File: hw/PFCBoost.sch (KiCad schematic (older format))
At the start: 15 parts

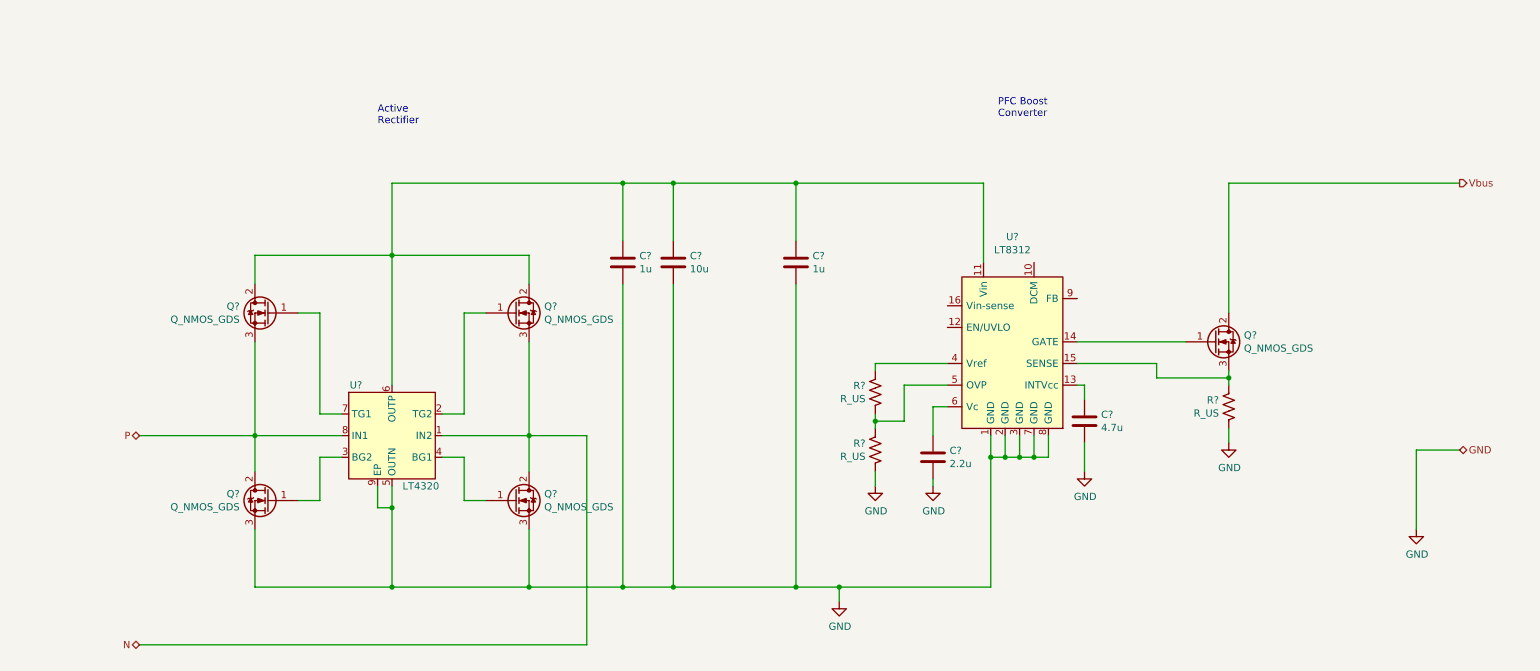
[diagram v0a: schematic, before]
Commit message: More work on PFC
Added more circuitry to PFC boost converter; about half done
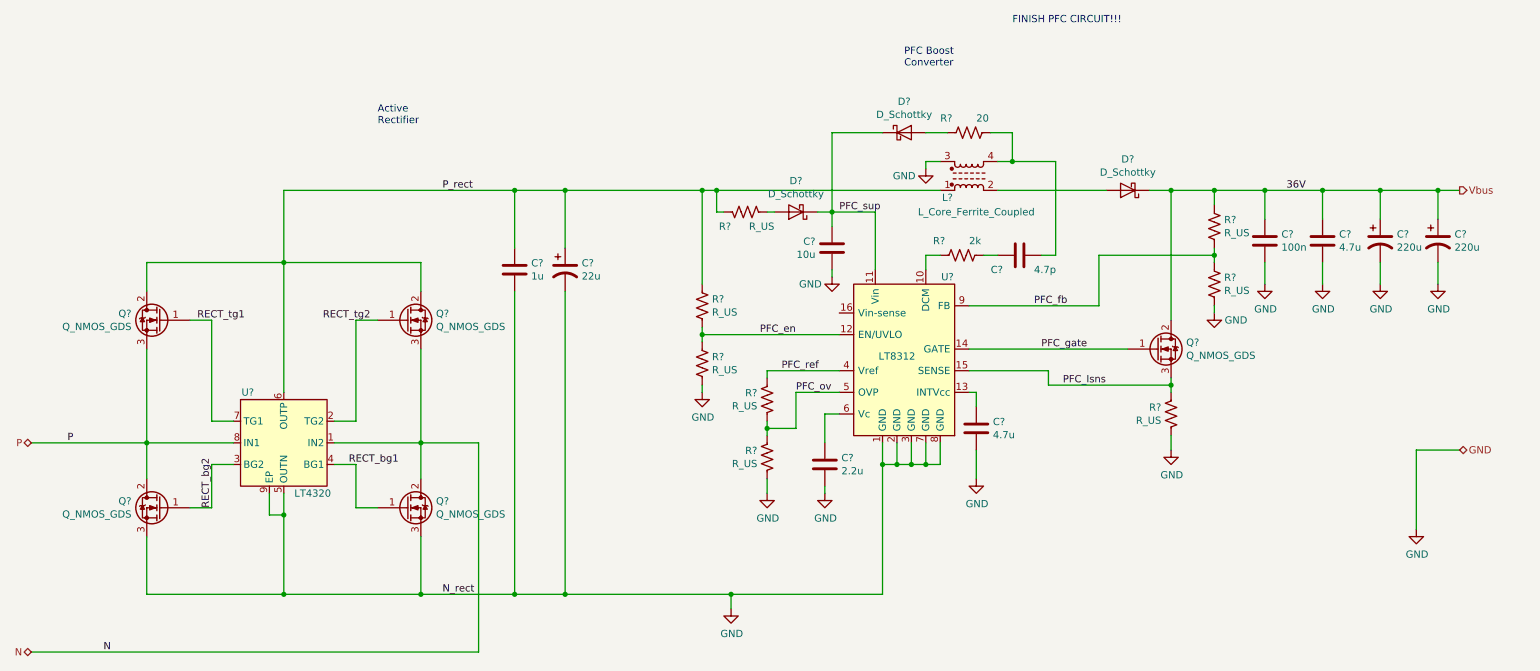
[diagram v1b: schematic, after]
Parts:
- removed C?: 10u, symbol Device:C
- removed C?: 1u, symbol Device:C
- added C?: 100n, Capacitor_SMD:C_0603_1608Metric, symbol Device:C
- added C? (x2): 220u, symbol Device:CP1
- added C?: 22u, symbol Device:CP1
- added C?: 4.7p, symbol Device:C
- added C?: 10u, Capacitor_SMD:C_1210_3225Metric_Pad1.42x2.65mm_HandSolder, symbol Device:C
- added C?: 4.7u, Capacitor_SMD:C_1210_3225Metric_Pad1.42x2.65mm_HandSolder, symbol Device:C
- added D?: D_Schottky, Diode_SMD:D_SMB, symbol Device:D_Schottky
- added D?: D_Schottky, symbol Device:D_Schottky
- added D?: D_Schottky, Diode_SMD:D_SOD-123, symbol Device:D_Schottky
- added L?: L_Core_Ferrite_Coupled, symbol Device:L_Core_Ferrite_Coupled
- added R? (x5): R_US, Resistor_SMD:R_0603_1608Metric, symbol Device:R_US
- added R?: 2k, Resistor_SMD:R_0603_1608Metric, symbol Device:R_US
- added R?: 20, Resistor_SMD:R_0603_1608Metric, symbol Device:R_US
- R?: footprint (none) -> Resistor_SMD:R_0612_1632Metric
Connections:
- net GND: now also C?.2, C?.2, C?.2, C?.2, C?.2, C?.2, L?.3, R?.1, R?.1
- net Vbus: now also C?.1, C?.1, C?.1, C?.1, D?.1 (K), R?.2
- net RECT_tg2: now reaches Q?.1 (G), U?.2 (TG2)
- net RECT_bg2: now reaches Q?.1 (G), U?.3 (BG2)
- net RECT_bg1: now reaches Q?.1 (G), U?.4 (BG1)
- net P_rect: now reaches C?.1, Q?.2 (D), Q?.2 (D), U?.6 (OUTP)
- net P_rect: now also C?.1, L?.1, R?.2, R?.2; no longer U?.11 (Vin)
- net RECT_tg1: now reaches Q?.1 (G), U?.7 (TG1)
- net at U?.10 (DCM): now also R?.1
- net PFC_en: now reaches U?.12 (EN/UVLO)
- net PFC_en: now also R?.1, R?.2
- net PFC_gate: now reaches Q?.1 (G), U?.14 (GATE)
- net PFC_Isns: now reaches Q?.3 (S), R?.2, U?.15 (SENSE)
- net PFC_ref: now reaches R?.2, U?.4 (Vref)
- net PFC_ov: now reaches R?.1, R?.2, U?.5 (OVP)
- net PFC_fb: now reaches U?.9 (FB)
- net PFC_fb: now also R?.1, R?.2
- new net: D?.2 (A), L?.2
- new net: C?.1, L?.4, R?.2
- new net: C?.2, R?.2
- new net: D?.2 (A), R?.1 (x2)
- new net PFC_sup: C?.1, D?.1 (K), D?.1 (K), U?.11 (Vin)
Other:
- note added: "FINISH PFC CIRCUIT!!!"
- moved on the sheet: C?, Q?, R?, U?

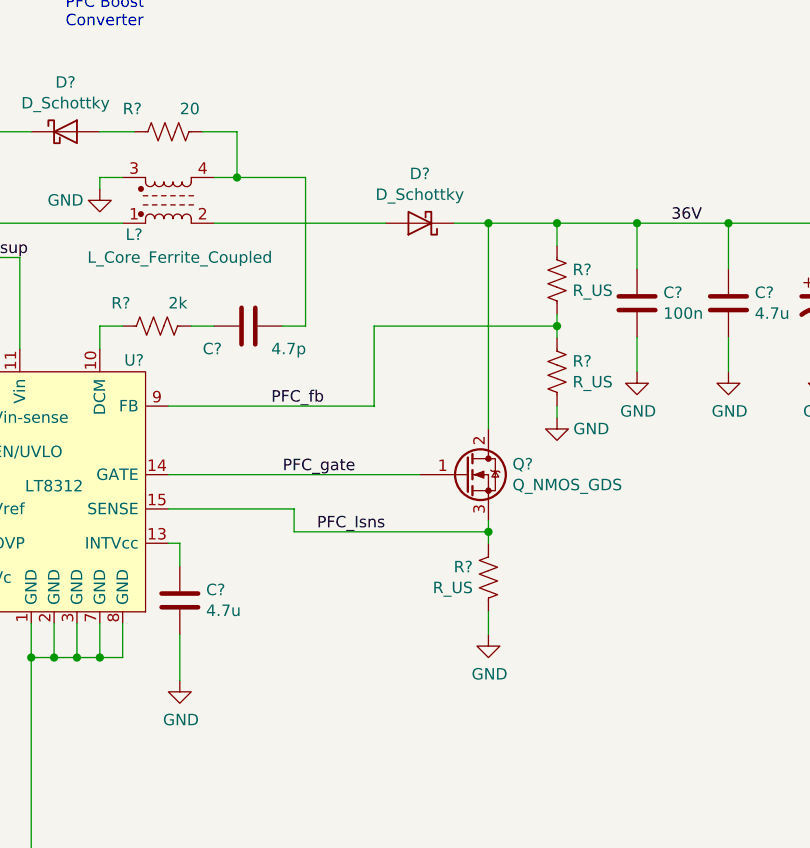
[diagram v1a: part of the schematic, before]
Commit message: Primary SW component selection
selected some components for primary switcher, added AuxOut block, dropped down primary linear reg IC
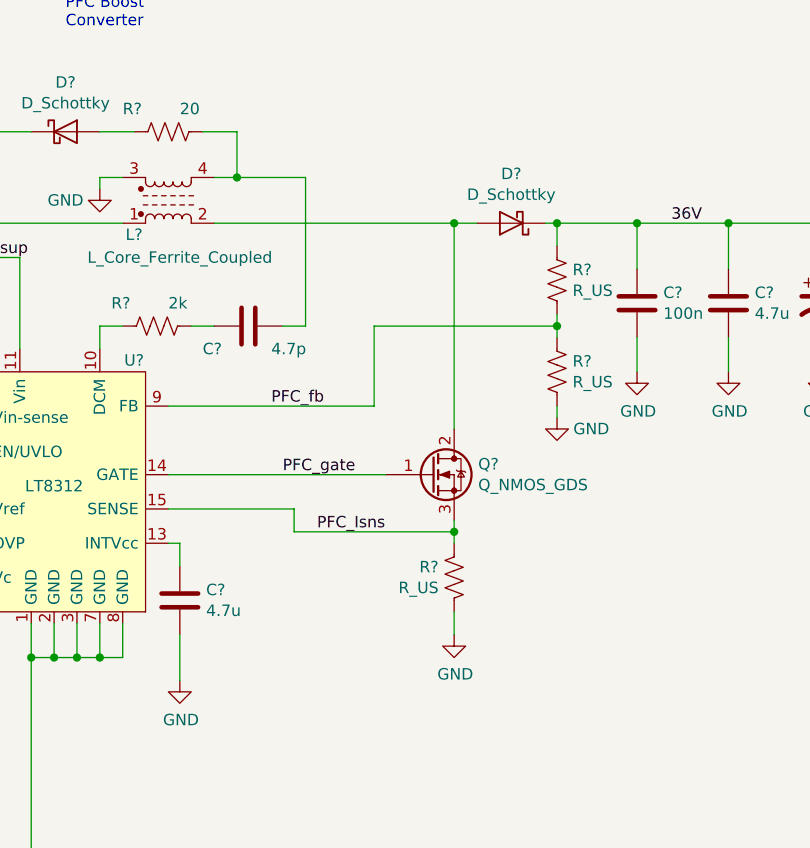
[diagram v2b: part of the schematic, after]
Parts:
- C?: footprint (none) -> Capacitor_SMD:C_0805_2012Metric
- C? (x2): footprint (none) -> Capacitor_SMD:C_0805_2012Metric_Pad1.15x1.40mm_HandSolder
- C?: footprint (none) -> Capacitor_SMD:C_0603_1608Metric
- D?: footprint (none) -> Diode_SMD:D_SOD-123
- R? (x2): footprint (none) -> Resistor_SMD:R_0603_1608Metric
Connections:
- net Vbus: no longer Q?.2 (D)
- net at D?.2 (A), L?.2: now also Q?.2 (D)
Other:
- moved on the sheet: D?, Q?, R?
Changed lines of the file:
@@
 $Descr A4 11693 8268
 encoding utf-8
-Sheet 2 6
+Sheet 2 7
 Title ""
 Date ""
@@
 F 0 "C?" H 4265 2546 50  0000 L CNN
 F 1 "1u" H 4265 2455 50  0000 L CNN
-F 2 "" H 4188 2350 50  0001 C CNN
+F 2 "Capacitor_SMD:C_0805_2012Metric" H 4188 2350 50  0001 C CNN
 F 3 "~" H 4150 2500 50  0001 C CNN
 	1    4150 2500
@@
 F 0 "C?" H 7465 3646 50  0000 L CNN
 F 1 "4.7u" H 7465 3555 50  0000 L CNN
-F 2 "" H 7388 3450 50  0001 C CNN
+F 2 "Capacitor_SMD:C_0805_2012Metric_Pad1.15x1.40mm_HandSolder" H 7388 3450 50  0001 C CNN
 F 3 "~" H 7350 3600 50  0001 C CNN
 	1    7350 3600
@@
 F 0 "R?" H 5832 3754 50  0000 R CNN
 F 1 "R_US" H 5832 3845 50  0000 R CNN
-F 2 "" V 5940 3790 50  0001 C CNN
+F 2 "Resistor_SMD:R_0603_1608Metric" V 5940 3790 50  0001 C CNN
 F 3 "~" H 5900 3800 50  0001 C CNN
 	1    5900 3800
@@
 F 0 "R?" H 5832 3354 50  0000 R CNN
 F 1 "R_US" H 5832 3445 50  0000 R CNN
-F 2 "" V 5940 3390 50  0001 C CNN
+F 2 "Resistor_SMD:R_0603_1608Metric" V 5940 3390 50  0001 C CNN
 F 3 "~" H 5900 3400 50  0001 C CNN
 	1    5900 3400
@@
 F 0 "C?" H 6415 3896 50  0000 L CNN
 F 1 "2.2u" H 6415 3805 50  0000 L CNN
-F 2 "" H 6338 3700 50  0001 C CNN
+F 2 "Capacitor_SMD:C_0805_2012Metric_Pad1.15x1.40mm_HandSolder" H 6338 3700 50  0001 C CNN
 F 3 "~" H 6300 3850 50  0001 C CNN
 	1    6300 3850
@@
 L Device:Q_NMOS_GDS Q?
 U 1 1 5E8395C3
-P 8600 3050
-F 0 "Q?" H 8805 3096 50  0000 L CNN
-F 1 "Q_NMOS_GDS" H 8805 3005 50  0000 L CNN
-F 2 "" H 8800 3150 50  0001 C CNN
-F 3 "~" H 8600 3050 50  0001 C CNN
-	1    8600 3050
+P 8450 3050
+F 0 "Q?" H 8655 3096 50  0000 L CNN
+F 1 "Q_NMOS_GDS" H 8655 3005 50  0000 L CNN
+F 2 "" H 8650 3150 50  0001 C CNN
+F 3 "~" H 8450 3050 50  0001 C CNN
+	1    8450 3050
 	1    0    0    -1
 $EndComp
@@
 L Device:R_US R?
 U 1 1 5E8396C6
-P 8700 3500
-F 0 "R?" H 8632 3454 50  0000 R CNN
-F 1 "R_US" H 8632 3545 50  0000 R CNN
-F 2 "Resistor_SMD:R_0612_1632Metric" V 8740 3490 50  0001 C CNN
-F 3 "~" H 8700 3500 50  0001 C CNN
-	1    8700 3500
+P 8550 3500
+F 0 "R?" H 8482 3454 50  0000 R CNN
+F 1 "R_US" H 8482 3545 50  0000 R CNN
+F 2 "Resistor_SMD:R_0612_1632Metric" V 8590 3490 50  0001 C CNN
+F 3 "~" H 8550 3500 50  0001 C CNN
+	1    8550 3500
 	1    0    0    1
 $EndComp
@@
 L power:GND #PWR?
 U 1 1 5E839706
-P 8700 3750
-F 0 "#PWR?" H 8700 3500 50  0001 C CNN
-F 1 "GND" H 8705 3577 50  0000 C CNN
-F 2 "" H 8700 3750 50  0001 C CNN
-F 3 "" H 8700 3750 50  0001 C CNN
-	1    8700 3750
-	1    0    0    -1
-$EndComp
-Wire Wire Line
-	8700 3250 8700 3300
-Wire Wire Line
-	7300 3050 8400 3050
-Wire Wire Line
-	8700 3300 7850 3300
+P 8550 3750
+F 0 "#PWR?" H 8550 3500 50  0001 C CNN
+F 1 "GND" H 8555 3577 50  0000 C CNN
+F 2 "" H 8550 3750 50  0001 C CNN
+F 3 "" H 8550 3750 50  0001 C CNN
+	1    8550 3750
+	1    0    0    -1
+$EndComp
+Wire Wire Line
+	8550 3250 8550 3300
+Wire Wire Line
+	7300 3050 8250 3050
+Wire Wire Line
+	8550 3300 7850 3300
 Wire Wire Line
 	7850 3300 7850 3200
 Wire Wire Line
 	7850 3200 7300 3200
-Connection ~ 8700 3300
-Wire Wire Line
-	8700 3300 8700 3350
-Wire Wire Line
-	8700 3650 8700 3750
+Connection ~ 8550 3300
+Wire Wire Line
+	8550 3300 8550 3350
+Wire Wire Line
+	8550 3650 8550 3750
 $Comp
 L power:GND #PWR?
@@
 	10400 3750 10700 3750
 Wire Wire Line
-	8700 2850 8700 1950
-Wire Wire Line
-	8700 1950 9000 1950
+	8550 2850 8550 1950
 Text HLabel 10700 1950 2    50   Output ~ 0
 Vbus
@@
 Wire Wire Line
 	9000 2050 9000 1950
-Connection ~ 9000 1950
 Wire Wire Line
 	9000 1950 9350 1950
@@
 	1    0    0    -1
 $EndComp
-$Comp
-L Device:L_Core_Ferrite_Coupled L?
-U 1 1 5EBA7662
-P 7300 1850
-F 0 "L?" H 7150 2000 50  0000 C CNN
-F 1 "L_Core_Ferrite_Coupled" H 7350 2100 50  0000 C CNN
-F 2 "" H 7300 1850 50  0001 C CNN
-F 3 "~" H 7300 1850 50  0001 C CNN
-	1    7300 1850
-	1    0    0    1
-$EndComp
 Wire Wire Line
 	5450 1950 5550 1950
-Wire Wire Line
-	7500 1950 8250 1950
-Wire Wire Line
-	8550 1950 8700 1950
-Connection ~ 8700 1950
 $Comp
 L Device:C C?
@@
 F 0 "C?" V 7750 2200 50  0000 L CNN
 F 1 "4.7p" V 7750 2500 50  0000 L CNN
-F 2 "" H 7688 2250 50  0001 C CNN
+F 2 "Capacitor_SMD:C_0603_1608Metric" H 7688 2250 50  0001 C CNN
 F 3 "~" H 7650 2400 50  0001 C CNN
 	1    7650 2400
@@
 Wire Wire Line
 	6350 2100 6350 2200
-$Comp
-L Device:D_Schottky D?
-U 1 1 5EC29700
-P 6850 1550
-F 0 "D?" H 6850 1766 50  0000 C CNN
-F 1 "D_Schottky" H 6850 1675 50  0000 C CNN
-F 2 "" H 6850 1550 50  0001 C CNN
-F 3 "~" H 6850 1550 50  0001 C CNN
-	1    6850 1550
-	1    0    0    -1
-$EndComp
 Wire Wire Line
 	7150 1550 7000 1550
@@
 L Device:D_Schottky D?
 U 1 1 5EBAA43A
-P 8400 1950
-F 0 "D?" H 8400 1734 50  0000 C CNN
-F 1 "D_Schottky" H 8400 1825 50  0000 C CNN
-F 2 "Diode_SMD:D_SMB" H 8400 1950 50  0001 C CNN
-F 3 "~" H 8400 1950 50  0001 C CNN
-	1    8400 1950
+P 8800 1950
+F 0 "D?" H 8800 1734 50  0000 C CNN
+F 1 "D_Schottky" H 8800 1825 50  0000 C CNN
+F 2 "Diode_SMD:D_SMB" H 8800 1950 50  0001 C CNN
+F 3 "~" H 8800 1950 50  0001 C CNN
+	1    8800 1950
 	-1   0    0    1
 $EndComp
@@
 Text Label 9500 1950 0    50   ~ 0
 36V
+Wire Wire Line
+	7500 1950 8550 1950
+Wire Wire Line
+	8650 1950 8550 1950
+Connection ~ 8550 1950
+Wire Wire Line
+	8950 1950 9000 1950
+Connection ~ 9000 1950
+$Comp
+L Device:D_Schottky D?
+U 1 1 5EC29700
+P 6850 1550
+F 0 "D?" H 6850 1766 50  0000 C CNN
+F 1 "D_Schottky" H 6850 1675 50  0000 C CNN
+F 2 "Diode_SMD:D_SOD-123" H 6850 1550 50  0001 C CNN
+F 3 "~" H 6850 1550 50  0001 C CNN
+	1    6850 1550
+	1    0    0    -1
+$EndComp
+$Comp
+L Device:L_Core_Ferrite_Coupled L?
+U 1 1 5EBA7662
+P 7300 1850
+F 0 "L?" H 7150 2000 50  0000 C CNN
+F 1 "L_Core_Ferrite_Coupled" H 7350 2100 50  0000 C CNN
+F 2 "" H 7300 1850 50  0001 C CNN
+F 3 "~" H 7300 1850 50  0001 C CNN
+	1    7300 1850
+	1    0    0    1
+$EndComp
 $EndSCHEMATC

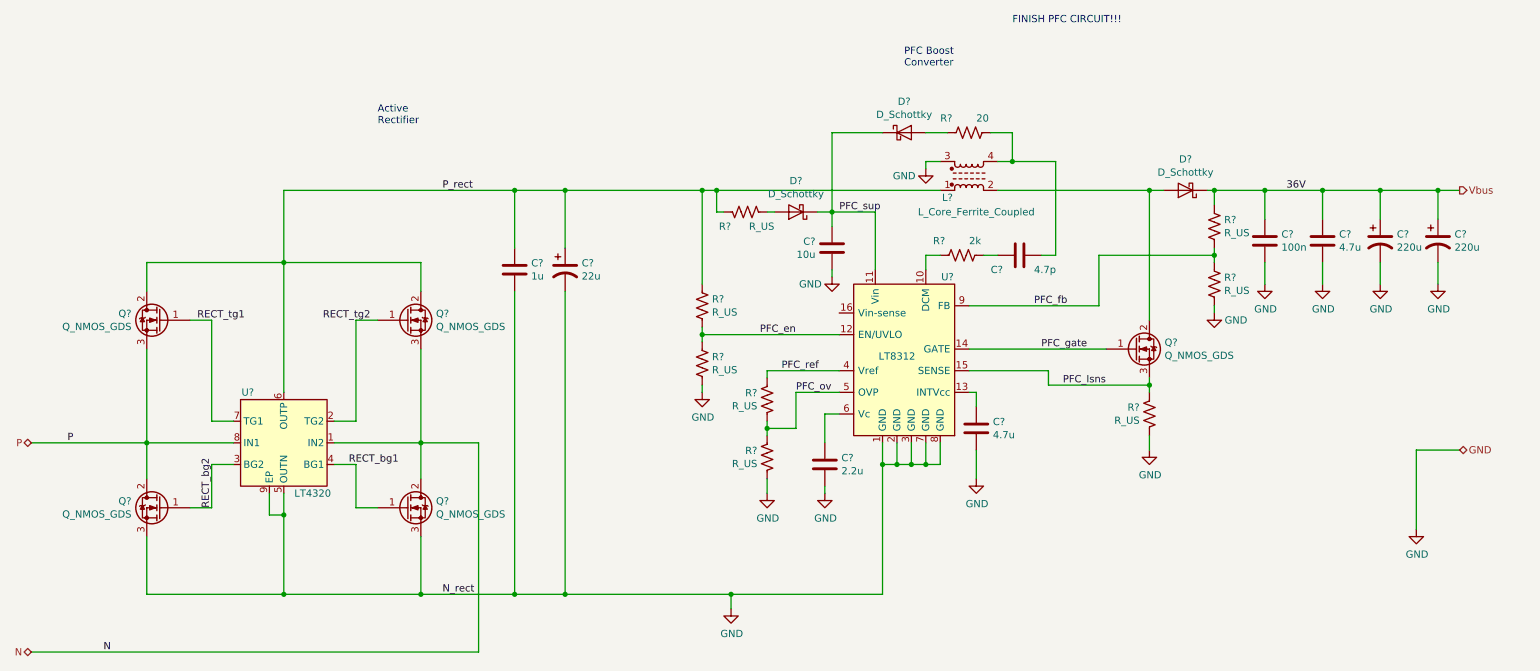
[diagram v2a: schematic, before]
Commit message: Cap selections
Lots of capacitor selections & datasheet downloads

Updated LTPowerCAD model with initial compensation values for primary switcher
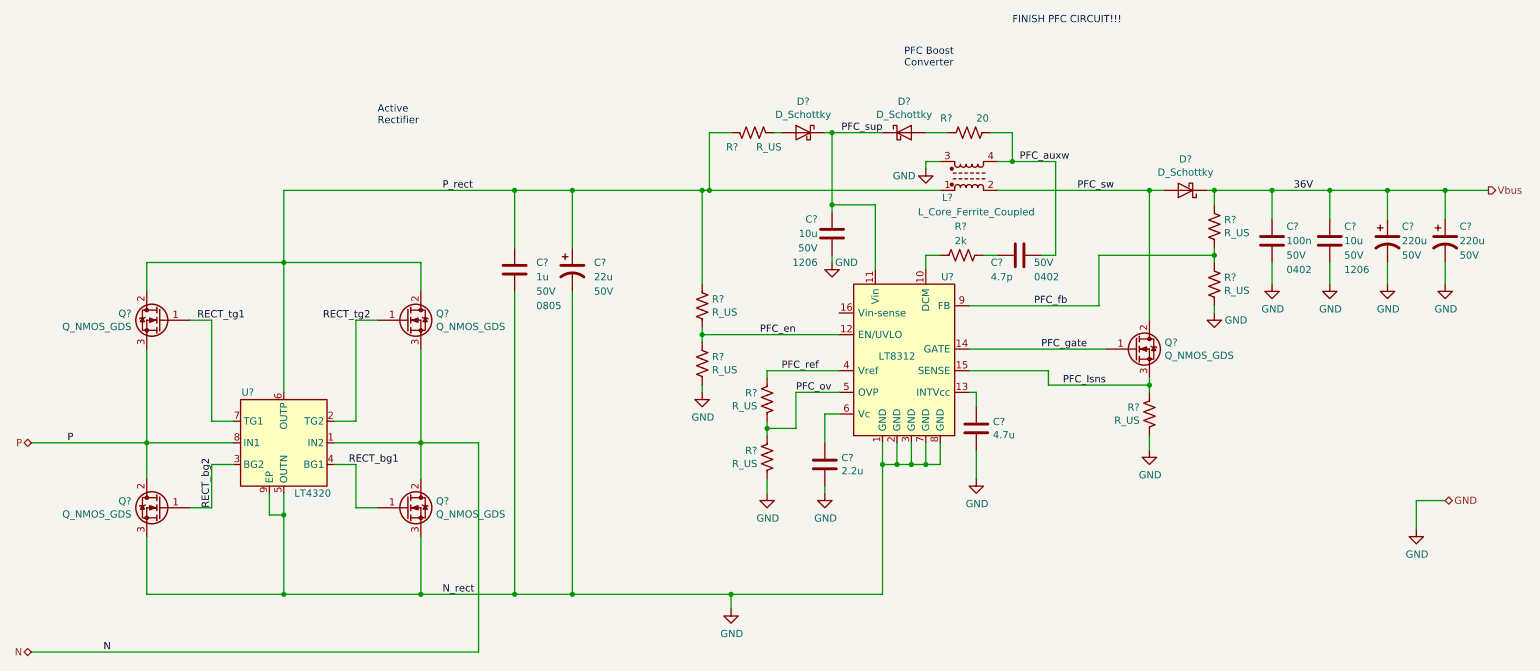
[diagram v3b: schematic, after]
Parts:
- removed C?: 100n, Capacitor_SMD:C_0603_1608Metric, symbol Device:C
- removed C?: 220u, symbol Device:CP1
- removed C?: 10u, Capacitor_SMD:C_1210_3225Metric_Pad1.42x2.65mm_HandSolder, symbol Device:C
- removed C?: 4.7u, Capacitor_SMD:C_1210_3225Metric_Pad1.42x2.65mm_HandSolder, symbol Device:C
- removed D?: D_Schottky, Diode_SMD:D_SOD-123, symbol Device:D_Schottky
- added C? (x2): 10u, Capacitor_SMD:C_1206_3216Metric_Pad1.42x1.75mm_HandSolder, symbol Device:C
- added C?: 100n, Capacitor_SMD:C_0603_1608Metric, symbol Device:C
- added C?: 220u, symbol Device:CP1
- added D?: D_Schottky, Diode_SMD:D_SOD-123, symbol Device:D_Schottky
- C?: MfrNum (none) -> TDK_C2012X5R1H105K125AB; Size (none) -> 0805; VRating (none) -> 50V
- C?: MfrNum (none) -> Panasonic_EEH-ZS1H221P; VRating (none) -> 50V
- C?: MfrNum (none) -> Panasonic_50SVPK22M; VRating (none) -> 50V
- C?: MfrNum (none) -> findapart; Size (none) -> 0402; VRating (none) -> 50V
- D?: IRating (none) -> 3A; VRating (none) -> 40V
- D?: IRating (none) -> 100mA; VRating (none) -> 40V
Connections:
- net GND: now also C?.2, C?.2, C?.2, C?.2
- net PFC_sup: now also C?.1, D?.1 (K)
- net Vbus: now also C?.1, C?.1, C?.1
- net PFC_sw: now reaches D?.2 (A), L?.2, Q?.2 (D)
- net PFC_auxw: now reaches C?.1, L?.4, R?.2
- net at R?.1: now also D?.2 (A)
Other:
- moved on the sheet: C?, R?
